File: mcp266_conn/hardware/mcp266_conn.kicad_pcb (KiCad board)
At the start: 2 copper layers, 83.2 x 40.5 mm, 19 parts, among them J1 conn_dsub_plug_15pos, J10 CAN, J11 CANL jumper, J12 CANH jumper, J2 CAN, J3 LS1, J4 LS2, J5 LS3, J6 LS4, J7 Enc1, J8 Enc2, J9 enc conn

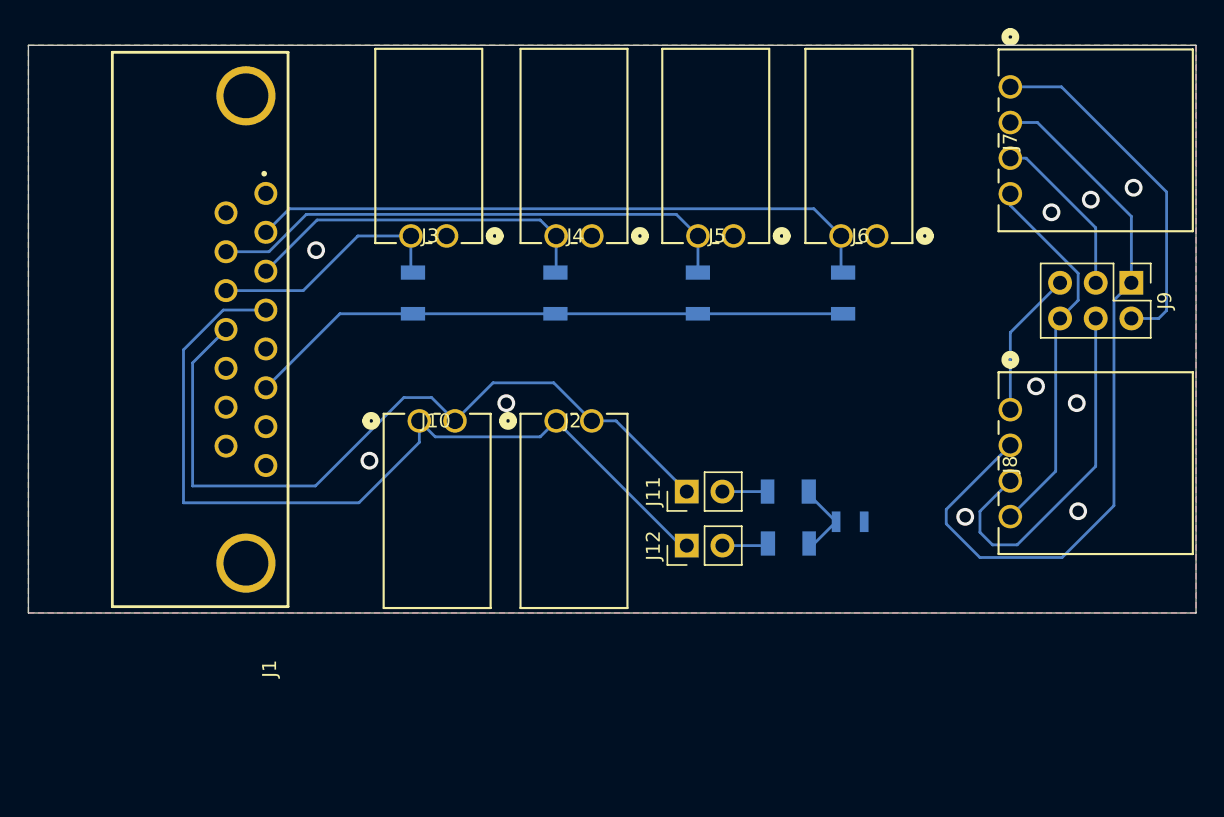
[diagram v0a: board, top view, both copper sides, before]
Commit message: design three seperate mcp connectors that can each dasiy chain for can, and one has limit switch headers and another the can termination
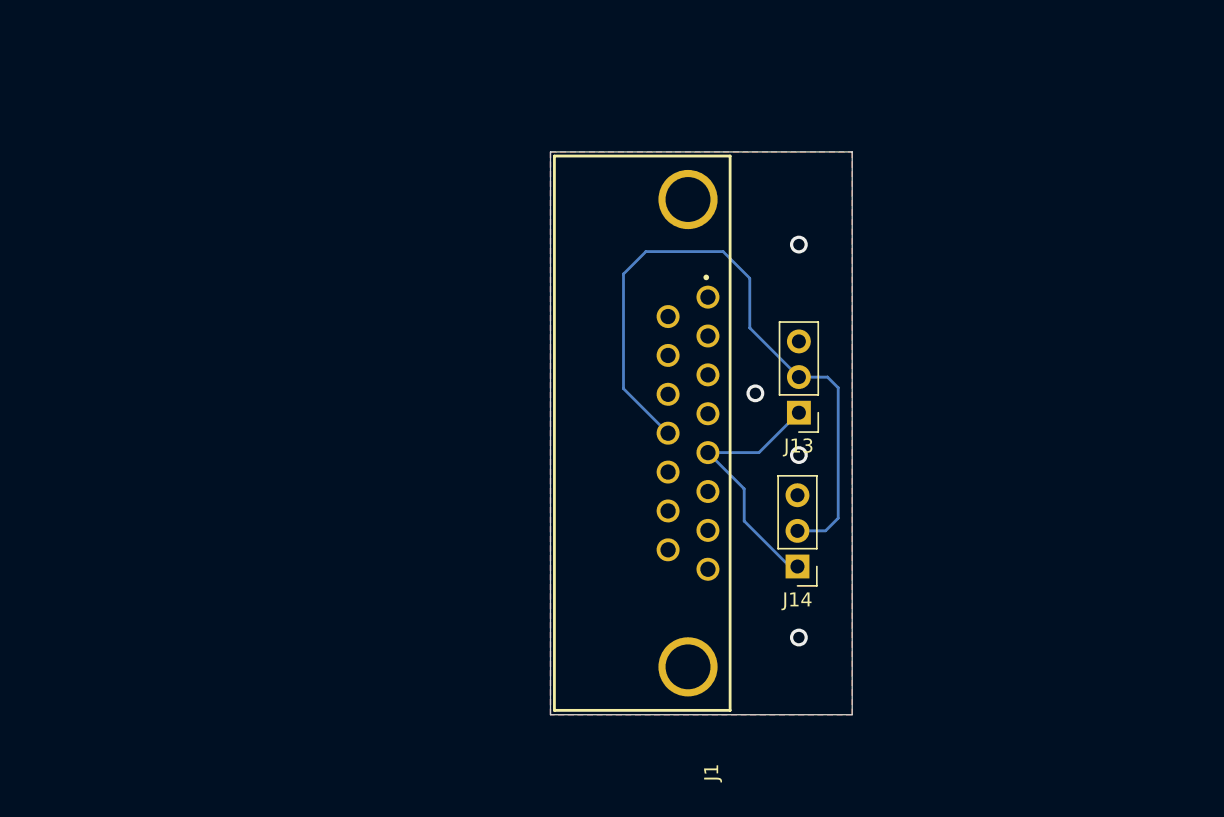
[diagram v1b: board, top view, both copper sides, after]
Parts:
- removed C1: 47nf, mcp266_conn:CAPC2012X145N
- removed J10, J2: CAN, mcp266_conn:HEADER90_2pin
- removed J11: CANL jumper, Connector_PinHeader_2.54mm:PinHeader_1x02_P2.54mm_Vertical
- removed J12: CANH jumper, Connector_PinHeader_2.54mm:PinHeader_1x02_P2.54mm_Vertical
- removed J3: LS1, mcp266_conn:HEADER90_2pin
- removed J4: LS2, mcp266_conn:HEADER90_2pin
- removed J5: LS3, mcp266_conn:HEADER90_2pin
- removed J6: LS4, mcp266_conn:HEADER90_2pin
- removed J7: Enc1, mcp266_conn:HEADER90_4pin
- removed J8: Enc2, mcp266_conn:HEADER90_4pin
- removed J9: enc conn, Connector_PinHeader_2.54mm:PinHeader_2x03_P2.54mm_Vertical
- removed R1, R6: 60, mcp266_conn:RESC3116X65N
- removed R2, R3, R4, R5: 5k, mcp266_conn:RESC3116X65N
- added J13: CAN, Connector_PinHeader_2.54mm:PinHeader_1x03_P2.54mm_Vertical, F.Cu at (134.5, 86.9)
- added J14: CAN, Connector_PinHeader_2.54mm:PinHeader_1x03_P2.54mm_Vertical, F.Cu at (134.4, 97.8)
- moved J1 32.4 mm to (120.3, 88.3)
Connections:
- J1 pad 10: /LS3 -> unconnected-(J1-Pad10)
- J1 pad 11: /LS1 -> unconnected-(J1-Pad11)
- J1 pad 2: /LS4 -> /GND
- J1 pad 3: /LS2 -> unconnected-(J1-Pad3)
- J1 pad 4: /CANH -> unconnected-(J1-Pad4)
- J1 pad 5: unconnected-(J1-Pad5) -> /CANH
- J1 pad 6: /5V -> unconnected-(J1-Pad6)
- J1 pad 7: GND -> unconnected-(J1-Pad7)
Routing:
- net /5V_enc: track 54.5 -> 0.00 mm
- net /LS4: track 44.8 -> 0.00 mm
- net /5V: track 43.4 -> 0.00 mm
- net /CANH: track 61.7 -> 18.7 mm
- net /LS3: track 37.8 -> 0.00 mm
- net /GND_enc: track 27.0 -> 0.00 mm
- net /2B: track 26.0 -> 0.00 mm
- net /1A: track 25.4 -> 0.00 mm
- net /LS2: track 25.2 -> 0.00 mm
- net /LS1: track 17.4 -> 0.00 mm
- net /1B: track 12.1 -> 0.00 mm
- net /2A: track 10.5 -> 0.00 mm
- net /CANL: track 55.0 -> 47.3 mm
- net Net-(C1-Pad2): track 5.52 -> 0.00 mm
- net /CANH_1: track 3.31 -> 0.00 mm
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- added copper zone on B.Cu, net /GND
- added copper zone on F.Cu, net /GND
- removed copper zone on B.Cu, net GND
- removed copper zone on F.Cu, net GND
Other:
- board size 83.2 x 40.5 mm -> 21.5 x 40.1 mm

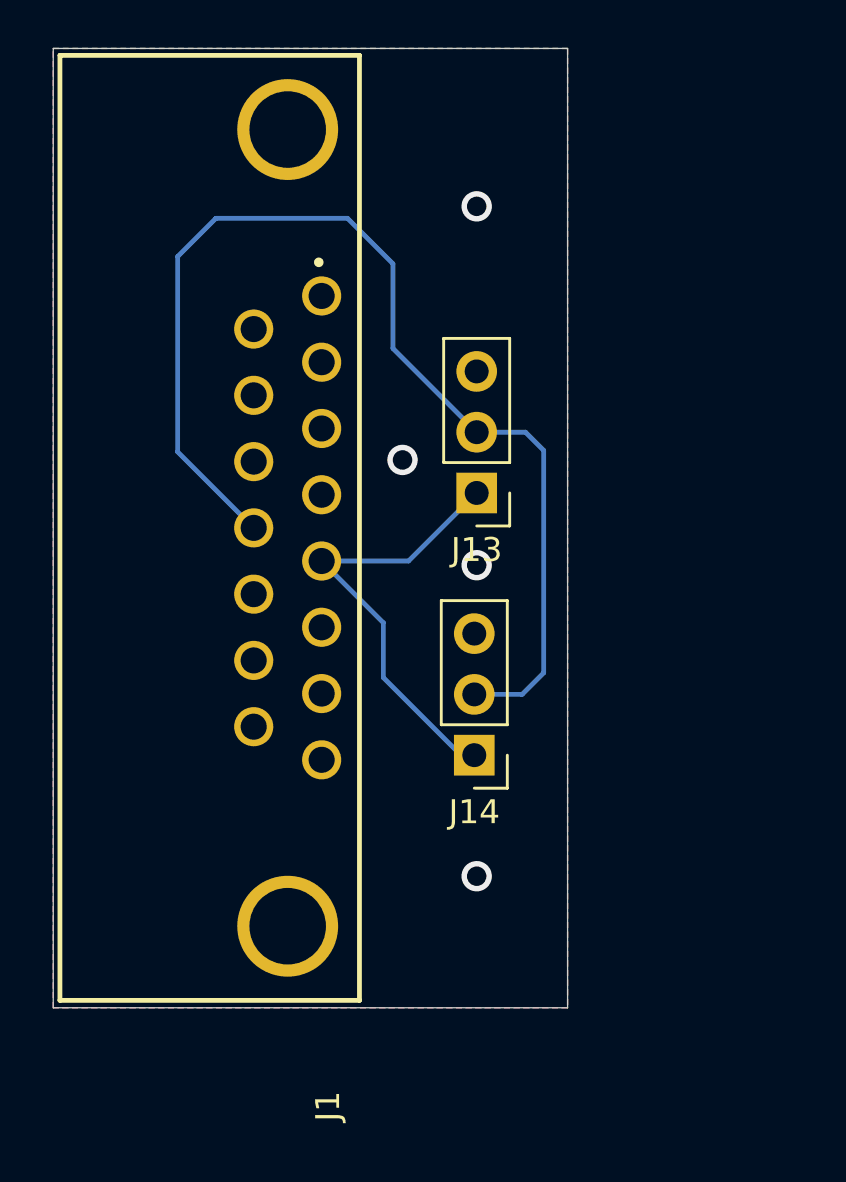
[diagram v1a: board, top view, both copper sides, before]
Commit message: made all in one mcp connector
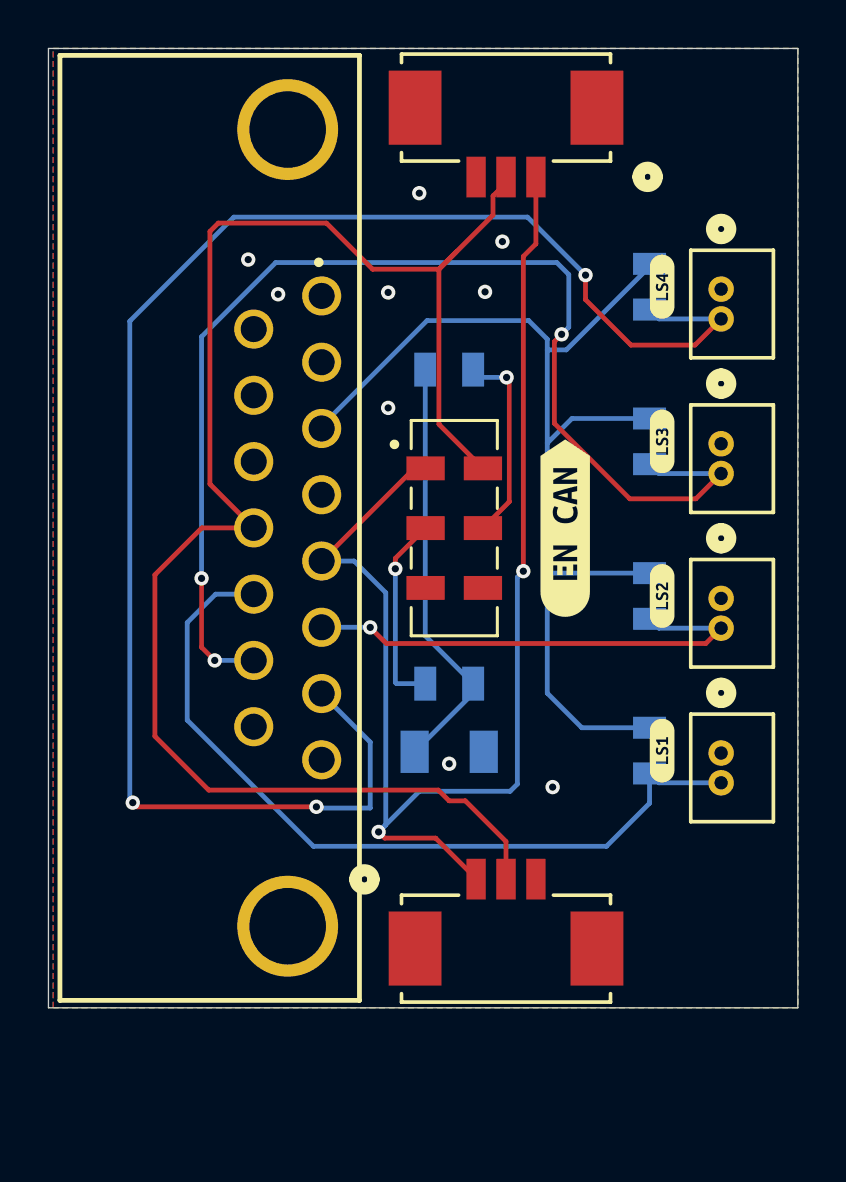
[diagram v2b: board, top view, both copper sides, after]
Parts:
- removed J13, J14: CAN, Connector_PinHeader_2.54mm:PinHeader_1x03_P2.54mm_Vertical
- added C1: 47nf, mcp266_conn:CAP_47nF, B.Cu at (133.3, 97.7)
- added J2: CONN_532610001-SD_03_MOL, mcp266_conn:CAN_HEADER_NEW, F.Cu at (135.7, 105.9)
- added J3: CONN_532610001-SD_03_MOL, mcp266_conn:CAN_HEADER_NEW, F.Cu at (135.7, 70.8)
- added J4: CONN02_530470210_MOL, mcp266_conn:LS_HEADER_NEW, F.Cu at (144.7, 97.8)
- added J5: CONN02_530470210_MOL, mcp266_conn:LS_HEADER_NEW, F.Cu at (144.7, 91.3)
- added J6: CONN02_530470210_MOL, mcp266_conn:LS_HEADER_NEW, F.Cu at (144.7, 84.8)
- added J7: CONN02_530470210_MOL, mcp266_conn:LS_HEADER_NEW, F.Cu at (144.7, 78.4)
- added R11: 1.2k, mcp266_conn:RES_1.2k, B.Cu at (141.7, 97.6)
- added R12: 1.2k, mcp266_conn:RES_1.2k, B.Cu at (141.7, 91.2)
- added R13: 1.2k, mcp266_conn:RES_1.2k, B.Cu at (141.7, 84.7)
- added R14: 1.2k, mcp266_conn:RES_1.2k, B.Cu at (141.7, 78.3)
- added R5: 60, mcp266_conn:RES_60.4ohms, B.Cu at (133.3, 94.8)
- added R6: 60, mcp266_conn:RES_60.4ohms, B.Cu at (133.3, 81.7)
- added S1: CAM_EN_switch, mcp266_conn:CAN_EN_switch, F.Cu at (133.6, 88.3)
- added kibuzzard-6AD7AD93: G***, kibuzzard-6AD7AD93, F.Cu at (138.2, 88.3)
- added kibuzzard-6AD7ADCE: G***, kibuzzard-6AD7ADCE, F.Cu at (142.2, 97.6)
- added kibuzzard-6AD7AE04: G***, kibuzzard-6AD7AE04, F.Cu at (142.2, 91.2)
- added kibuzzard-6AD7AE10: G***, kibuzzard-6AD7AE10, F.Cu at (142.2, 84.7)
- added kibuzzard-6AD7AE1D: G***, kibuzzard-6AD7AE1D, F.Cu at (142.2, 78.3)
- J1: value conn_dsub_plug_15pos -> 618015211721
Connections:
- J1 pad 13: unconnected-(J1-Pad13) -> /LS1
- J1 pad 14: unconnected-(J1-Pad14) -> /LS3
- J1 pad 3: unconnected-(J1-Pad3) -> /5V
- J1 pad 6: unconnected-(J1-Pad6) -> /LS2
- J1 pad 7: unconnected-(J1-Pad7) -> /LS4
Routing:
- net /LS4: track 0.00 -> 68.8 mm, vias 0 -> 3
- net /LS3: track 0.00 -> 50.6 mm, vias 0 -> 3
- net /5V: track 0.00 -> 46.2 mm
- net /CANH: track 18.7 -> 56.5 mm, vias 0 -> 2
- net /LS1: track 0.00 -> 34.0 mm
- net /CANL: track 47.3 -> 68.5 mm
- net /LS2: track 0.00 -> 20.4 mm, vias 0 -> 1
- net Net-(C1-Pad2): track 0.00 -> 17.4 mm
- net /CANL_1: track 0.00 -> 8.41 mm, vias 0 -> 1
- net /CANH_1: track 0.00 -> 8.24 mm, vias 0 -> 1
- net /GND: track 0.54 -> 0.00 mm, vias 4 -> 9
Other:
- board size 21.5 x 40.1 mm -> 31.3 x 40.1 mm

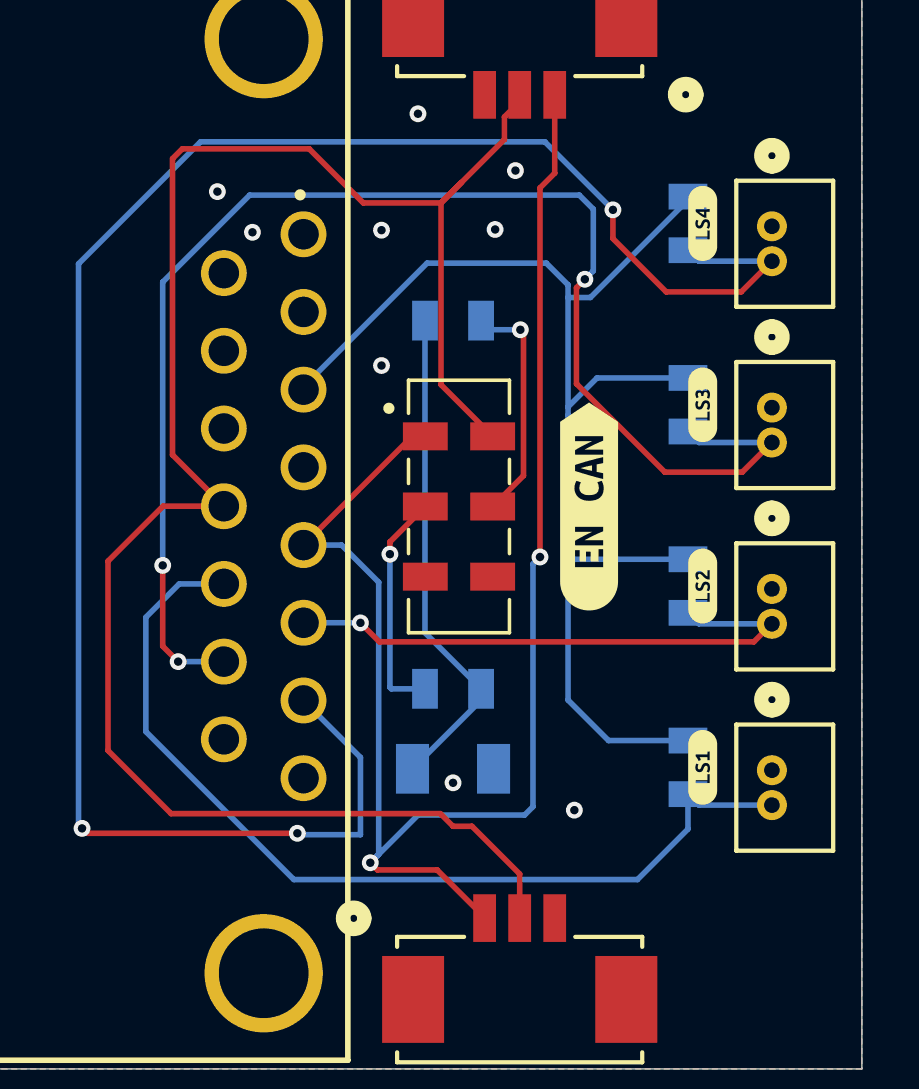
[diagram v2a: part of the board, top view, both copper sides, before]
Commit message: created mcp conn for just bare board build at jlc
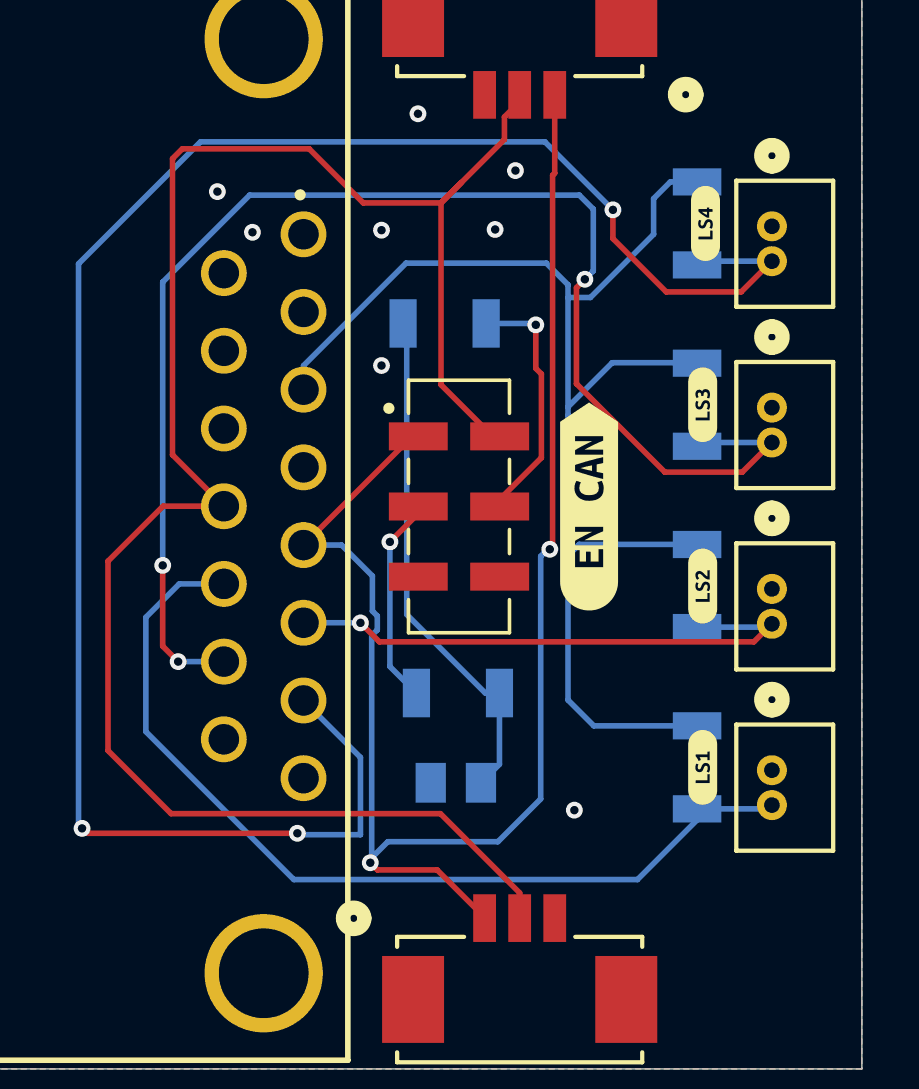
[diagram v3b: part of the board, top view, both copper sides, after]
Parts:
- C1: footprint mcp266_conn:CAP_47nF -> mcp266_conn:CAP_size_0805
- R11, R12, R13, R14: footprint mcp266_conn:RES_1.2k -> mcp266_conn:RES_size_1206
- R5, R6: footprint mcp266_conn:RES_60.4ohms -> mcp266_conn:RES_size_1206
- moved C1 0.51 mm to (133.4, 98.2), turned to 0 degrees
- moved R11 0.33 mm to (142.1, 97.6)
- moved R12 0.33 mm to (142.1, 91.2)
- moved R13 0.33 mm to (142.1, 84.7)
- moved R14 0.33 mm to (142.1, 78.3)
- moved R6 0.32 mm to (133.1, 81.8)
- moved R5 0.23 mm to (133.5, 95.0)
- moved kibuzzard-6AD7AE1D 0.10 mm to (142.3, 78.3)
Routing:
- net /5V: track 46.2 -> 49.2 mm
- net /CANL_1: track 8.41 -> 9.53 mm
- net Net-(C1-Pad2): track 17.4 -> 18.4 mm
- net /LS1: track 34.0 -> 33.2 mm
- net /CANH_1: track 8.24 -> 7.56 mm
- net /LS4: track 68.8 -> 68.1 mm
- net /LS3: track 50.6 -> 50.0 mm
- net /GND: vias 9 -> 8

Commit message: files saved
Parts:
- J1: value 618015211721 -> conn_dsub_plug_15pos
- J2, J3: value CONN_532610001-SD_03_MOL -> CAN_HEADER_NEW
- J4, J5, J6, J7: value CONN02_530470210_MOL -> LS_HEADER_NEW
- moved S1 0.38 mm to (133.9, 88.2)
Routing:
- net /GND: vias 8 -> 9
